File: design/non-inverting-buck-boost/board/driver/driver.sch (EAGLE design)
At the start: 11 parts, among them IC1 L7812, IC2 78L05, T1 BC547

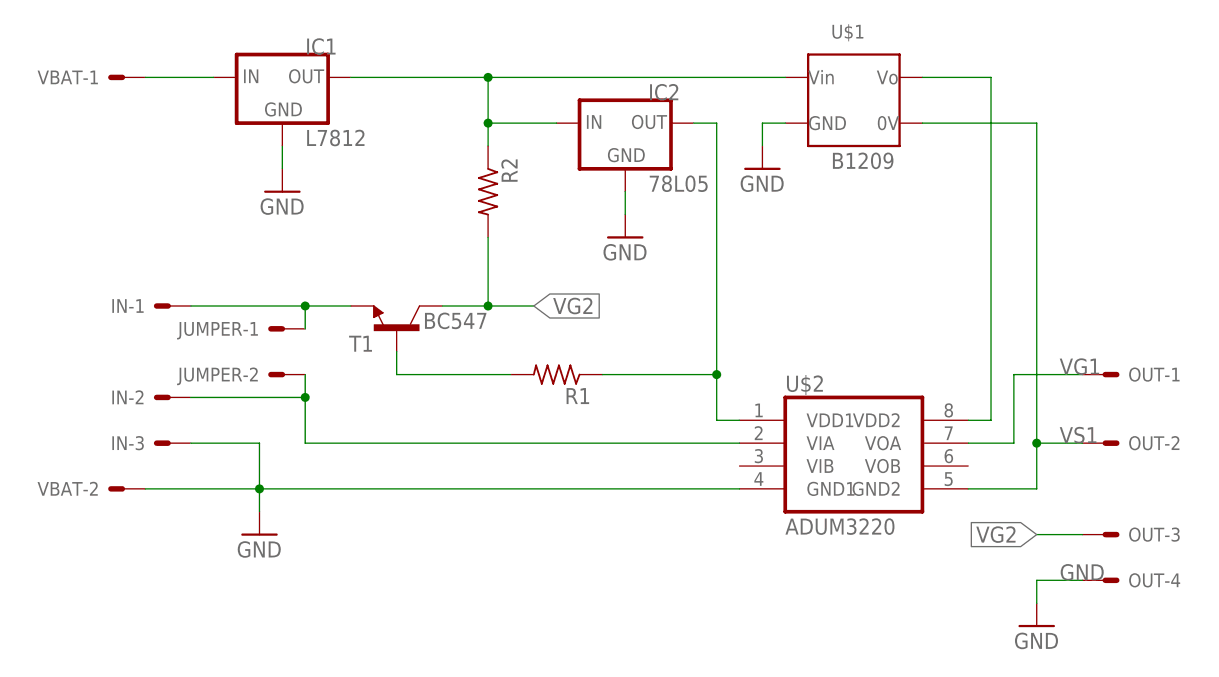
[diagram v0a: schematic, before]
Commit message: new driver design with 2 ADUM3220
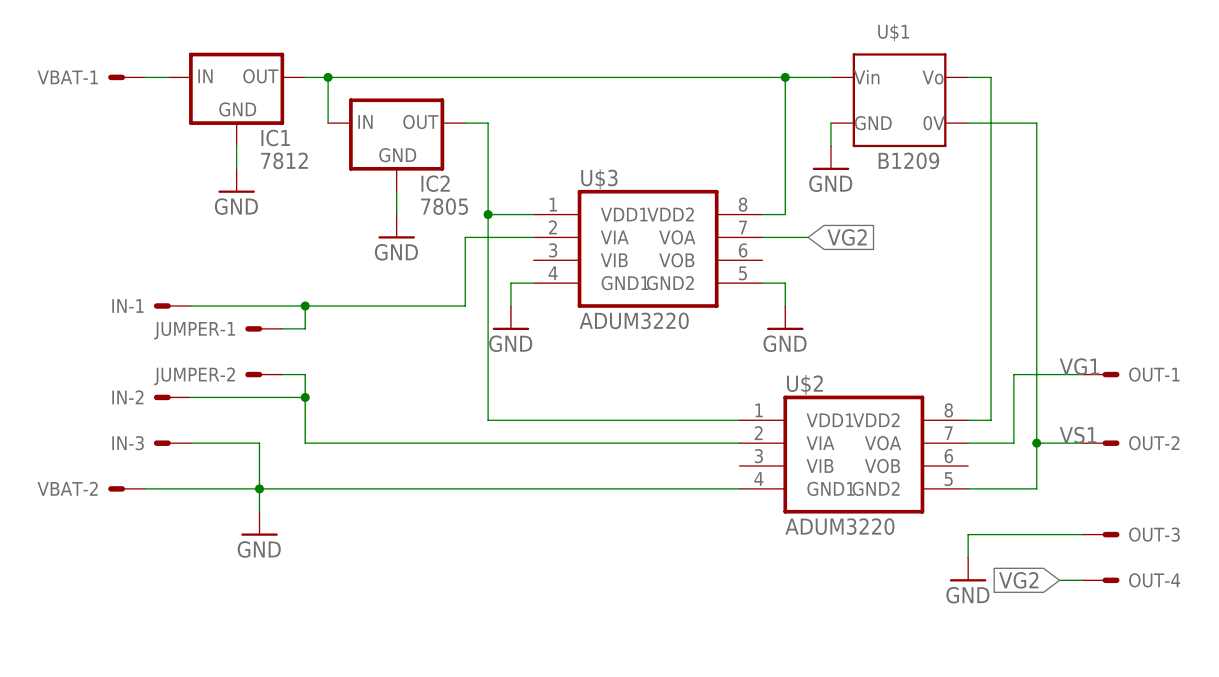
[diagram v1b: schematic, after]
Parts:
- removed R1, R2: (no value), resistor:R-US_0204/7
- removed T1: BC547, transistor:BC547
- added U$3: ADUM3220, felippe:ADUM3220
- IC1: value L7812 -> 7812; device v-reg:78XXL -> v-reg:78XXS
- IC2: value 78L05 -> 7805; device v-reg:78LXX -> v-reg:78XXS
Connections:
- removed net N$1: IC1.OUT, IC2.IN, R2.1, U$1.VIN
- removed net N$2: IC2.OUT, R1.1, U$2.VDD1
- removed net N$4: R1.2, T1.B
- new net 12V: IC1.OUT, IC2.IN, U$1.VIN, U$3.VDD2
- new net 5V: IC2.OUT, U$2.VDD1, U$3.VDD1
- net GND: now also OUT-3.S, U$3.GND1, U$3.GND2; no longer OUT-4.S
- net N$7: now also U$3.VIA; no longer T1.E
- net VG2: now also OUT-4.S, U$3.VOA; no longer OUT-3.S, R2.2, T1.C
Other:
- moved on the sheet: IC2, JUMPER-1, JUMPER-2, U$1

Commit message: changed non-isolated driver to TC4422
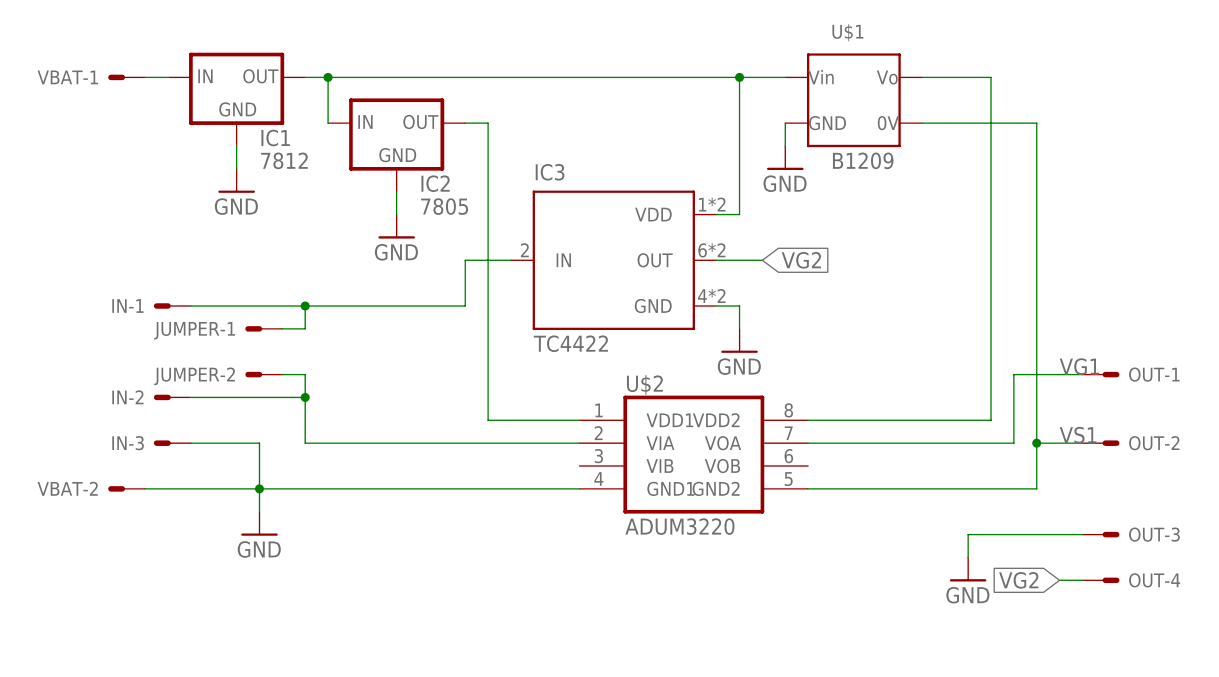
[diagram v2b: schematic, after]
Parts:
- removed U$3: ADUM3220, felippe:ADUM3220
- added IC3: TC4422, felippe:TC4422
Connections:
- net 12V: now also IC3.VDD; no longer U$3.VDD2
- net 5V: no longer U$3.VDD1
- net GND: now also IC3.GND; no longer U$3.GND1, U$3.GND2
- net N$7: now also IC3.IN; no longer U$3.VIA
- net VG2: now also IC3.OUT; no longer U$3.VOA
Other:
- moved on the sheet: U$1, U$2
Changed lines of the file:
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@@
 <part name="IN" library="con-molex" deviceset="22-23-2031" device=""/>
 <part name="JUMPER" library="con-molex" deviceset="22-23-2021" device=""/>
-<part name="U$3" library="felippe" deviceset="ADUM3220" device=""/>
-<part name="GND6" library="supply1" deviceset="GND" device=""/>
 <part name="GND7" library="supply1" deviceset="GND" device=""/>
 <part name="IC2" library="v-reg" deviceset="78XXS" device="" value="7805"/>
 <part name="IC1" library="v-reg" deviceset="78XXS" device="" value="7812"/>
+<part name="IC3" library="felippe" deviceset="TC4422" device=""/>
 </parts>
 <sheets>
@@
 </plain>
 <instances>
-<instance part="U$2" gate="G$1" x="68.58" y="30.48"/>
-<instance part="U$1" gate="G$1" x="73.66" y="73.66"/>
+<instance part="U$2" gate="G$1" x="50.8" y="30.48"/>
+<instance part="U$1" gate="G$1" x="68.58" y="73.66"/>
 <instance part="VBAT" gate="-1" x="-12.7" y="73.66" smashed="yes" rot="R180">
 <attribute name="NAME" x="-15.24" y="74.422" size="1.524" layer="95" rot="R180"/>
@@
 <instance part="VBAT" gate="-2" x="-12.7" y="27.94" rot="R180"/>
 <instance part="GND1" gate="1" x="2.54" y="22.86"/>
-<instance part="GND2" gate="1" x="66.04" y="63.5"/>
+<instance part="GND2" gate="1" x="60.96" y="63.5"/>
 <instance part="GND3" gate="1" x="0" y="60.96"/>
 <instance part="GND4" gate="1" x="17.78" y="55.88"/>
@@
 </instance>
 <instance part="JUMPER" gate="-2" x="2.54" y="40.64" rot="R180"/>
-<instance part="U$3" gate="G$1" x="45.72" y="53.34"/>
-<instance part="GND6" gate="1" x="30.48" y="45.72"/>
-<instance part="GND7" gate="1" x="60.96" y="45.72"/>
+<instance part="GND7" gate="1" x="55.88" y="43.18"/>
 <instance part="IC2" gate="1" x="17.78" y="68.58"/>
 <instance part="IC1" gate="1" x="0" y="73.66"/>
+<instance part="IC3" gate="P" x="40.64" y="53.34"/>
 </instances>
 <busses>
@@
 <segment>
 <pinref part="U$1" gate="G$1" pin="VIN"/>
-<wire x1="66.04" y1="73.66" x2="60.96" y2="73.66" width="0.1524" layer="91"/>
-<wire x1="60.96" y1="73.66" x2="10.16" y2="73.66" width="0.1524" layer="91"/>
+<wire x1="60.96" y1="73.66" x2="55.88" y2="73.66" width="0.1524" layer="91"/>
+<wire x1="55.88" y1="73.66" x2="10.16" y2="73.66" width="0.1524" layer="91"/>
 <wire x1="10.16" y1="73.66" x2="7.62" y2="73.66" width="0.1524" layer="91"/>
 <wire x1="10.16" y1="68.58" x2="10.16" y2="73.66" width="0.1524" layer="91"/>
 <junction x="10.16" y="73.66"/>
-<pinref part="U$3" gate="G$1" pin="VDD2"/>
-<wire x1="58.42" y1="58.42" x2="60.96" y2="58.42" width="0.1524" layer="91"/>
-<wire x1="60.96" y1="58.42" x2="60.96" y2="73.66" width="0.1524" layer="91"/>
-<junction x="60.96" y="73.66"/>
+<wire x1="55.88" y1="58.42" x2="55.88" y2="73.66" width="0.1524" layer="91"/>
+<junction x="55.88" y="73.66"/>
 <pinref part="IC2" gate="1" pin="IN"/>
 <pinref part="IC1" gate="1" pin="OUT"/>
+<pinref part="IC3" gate="P" pin="VDD"/>
+<wire x1="53.34" y1="58.42" x2="55.88" y2="58.42" width="0.1524" layer="91"/>
 </segment>
 </net>
@@
 <segment>
 <wire x1="25.4" y1="68.58" x2="27.94" y2="68.58" width="0.1524" layer="91"/>
-<wire x1="27.94" y1="68.58" x2="27.94" y2="58.42" width="0.1524" layer="91"/>
 <pinref part="U$2" gate="G$1" pin="VDD1"/>
-<wire x1="27.94" y1="58.42" x2="27.94" y2="35.56" width="0.1524" layer="91"/>
-<wire x1="27.94" y1="35.56" x2="55.88" y2="35.56" width="0.1524" layer="91"/>
-<pinref part="U$3" gate="G$1" pin="VDD1"/>
-<wire x1="33.02" y1="58.42" x2="27.94" y2="58.42" width="0.1524" layer="91"/>
-<junction x="27.94" y="58.42"/>
+<wire x1="27.94" y1="68.58" x2="27.94" y2="35.56" width="0.1524" layer="91"/>
+<wire x1="27.94" y1="35.56" x2="38.1" y2="35.56" width="0.1524" layer="91"/>
 <pinref part="IC2" gate="1" pin="OUT"/>
 </segment>
@@
 <segment>
 <pinref part="U$1" gate="G$1" pin="VO"/>
-<wire x1="81.28" y1="73.66" x2="83.82" y2="73.66" width="0.1524" layer="91"/>
+<wire x1="76.2" y1="73.66" x2="83.82" y2="73.66" width="0.1524" layer="91"/>
 <wire x1="83.82" y1="73.66" x2="83.82" y2="35.56" width="0.1524" layer="91"/>
 <pinref part="U$2" gate="G$1" pin="VDD2"/>
-<wire x1="83.82" y1="35.56" x2="81.28" y2="35.56" width="0.1524" layer="91"/>
+<wire x1="83.82" y1="35.56" x2="63.5" y2="35.56" width="0.1524" layer="91"/>
 </segment>
 </net>
@@
 <segment>
 <pinref part="U$1" gate="G$1" pin="0V"/>
-<wire x1="81.28" y1="68.58" x2="88.9" y2="68.58" width="0.1524" layer="91"/>
+<wire x1="76.2" y1="68.58" x2="88.9" y2="68.58" width="0.1524" layer="91"/>
 <wire x1="88.9" y1="68.58" x2="88.9" y2="33.02" width="0.1524" layer="91"/>
 <pinref part="U$2" gate="G$1" pin="GND2"/>
 <wire x1="88.9" y1="33.02" x2="88.9" y2="27.94" width="0.1524" layer="91"/>
-<wire x1="88.9" y1="27.94" x2="81.28" y2="27.94" width="0.1524" layer="91"/>
+<wire x1="88.9" y1="27.94" x2="63.5" y2="27.94" width="0.1524" layer="91"/>
 <pinref part="OUT" gate="-2" pin="S"/>
 <wire x1="93.98" y1="33.02" x2="88.9" y2="33.02" width="0.1524" layer="91"/>
@@
 <pinref part="VBAT" gate="-2" pin="S"/>
 <wire x1="-10.16" y1="27.94" x2="2.54" y2="27.94" width="0.1524" layer="91"/>
-<wire x1="2.54" y1="27.94" x2="55.88" y2="27.94" width="0.1524" layer="91"/>
+<wire x1="2.54" y1="27.94" x2="38.1" y2="27.94" width="0.1524" layer="91"/>
 <pinref part="U$2" gate="G$1" pin="GND1"/>
 <pinref part="GND1" gate="1" pin="GND"/>
@@
 <segment>
 <pinref part="GND2" gate="1" pin="GND"/>
-<wire x1="66.04" y1="66.04" x2="66.04" y2="68.58" width="0.1524" layer="91"/>
+<wire x1="60.96" y1="66.04" x2="60.96" y2="68.58" width="0.1524" layer="91"/>
 <pinref part="U$1" gate="G$1" pin="GND"/>
 </segment>
 <segment>
-<pinref part="GND6" gate="1" pin="GND"/>
-<wire x1="30.48" y1="48.26" x2="30.48" y2="50.8" width="0.1524" layer="91"/>
-<pinref part="U$3" gate="G$1" pin="GND1"/>
-<wire x1="30.48" y1="50.8" x2="33.02" y2="50.8" width="0.1524" layer="91"/>
-</segment>
-<segment>
-<pinref part="U$3" gate="G$1" pin="GND2"/>
 <pinref part="GND7" gate="1" pin="GND"/>
-<wire x1="58.42" y1="50.8" x2="60.96" y2="50.8" width="0.1524" layer="91"/>
-<wire x1="60.96" y1="50.8" x2="60.96" y2="48.26" width="0.1524" layer="91"/>
+<wire x1="55.88" y1="48.26" x2="55.88" y2="45.72" width="0.1524" layer="91"/>
+<pinref part="IC3" gate="P" pin="GND"/>
+<wire x1="53.34" y1="48.26" x2="55.88" y2="48.26" width="0.1524" layer="91"/>
 </segment>
 <segment>
@@
 <wire x1="7.62" y1="40.64" x2="7.62" y2="38.1" width="0.1524" layer="91"/>
 <wire x1="7.62" y1="38.1" x2="7.62" y2="33.02" width="0.1524" layer="91"/>
-<wire x1="7.62" y1="33.02" x2="55.88" y2="33.02" width="0.1524" layer="91"/>
+<wire x1="7.62" y1="33.02" x2="38.1" y2="33.02" width="0.1524" layer="91"/>
 <pinref part="IN" gate="-2" pin="S"/>
 <wire x1="-5.08" y1="38.1" x2="7.62" y2="38.1" width="0.1524" layer="91"/>
@@
 <net name="N$7" class="0">
 <segment>
-<pinref part="U$3" gate="G$1" pin="VIA"/>
-<wire x1="33.02" y1="55.88" x2="25.4" y2="55.88" width="0.1524" layer="91"/>
-<wire x1="25.4" y1="55.88" x2="25.4" y2="48.26" width="0.1524" layer="91"/>
+<wire x1="30.48" y1="53.34" x2="25.4" y2="53.34" width="0.1524" layer="91"/>
+<wire x1="25.4" y1="53.34" x2="25.4" y2="48.26" width="0.1524" layer="91"/>
 <wire x1="25.4" y1="48.26" x2="7.62" y2="48.26" width="0.1524" layer="91"/>
 <wire x1="7.62" y1="45.72" x2="7.62" y2="48.26" width="0.1524" layer="91"/>
@@
 <wire x1="-5.08" y1="48.26" x2="7.62" y2="48.26" width="0.1524" layer="91"/>
 <junction x="7.62" y="48.26"/>
+<pinref part="IC3" gate="P" pin="IN"/>
 </segment>
 </net>
 <net name="VG2" class="0">
 <segment>
-<pinref part="U$3" gate="G$1" pin="VOA"/>
-<wire x1="58.42" y1="55.88" x2="63.5" y2="55.88" width="0.1524" layer="91"/>
-<label x="63.5" y="55.88" size="1.778" layer="95" xref="yes"/>
+<label x="58.42" y="53.34" size="1.778" layer="95" xref="yes"/>
+<pinref part="IC3" gate="P" pin="OUT"/>
+<wire x1="58.42" y1="53.34" x2="53.34" y2="53.34" width="0.1524" layer="91"/>
 </segment>
 <segment>
@@
 <wire x1="86.36" y1="40.64" x2="86.36" y2="33.02" width="0.1524" layer="91"/>
 <pinref part="U$2" gate="G$1" pin="VOA"/>
-<wire x1="86.36" y1="33.02" x2="81.28" y2="33.02" width="0.1524" layer="91"/>
+<wire x1="86.36" y1="33.02" x2="63.5" y2="33.02" width="0.1524" layer="91"/>
 <label x="91.44" y="40.64" size="1.778" layer="95"/>
 </segment>
